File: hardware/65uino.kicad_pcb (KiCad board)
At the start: 2 copper layers, 75.4 x 53.6 mm, 50 parts, among them J1 Barrel_Jack_MountingPin, J2 USB_B_Micro, J3 OLED, SW1 RST, SW2 BTN, U1 R6507, U2 74HC04, U3 6532, U4 w27C512, U5 MIC5504-3.3YM5, U6 LM1117-5.0, X1 NC, Y1 1Mhz

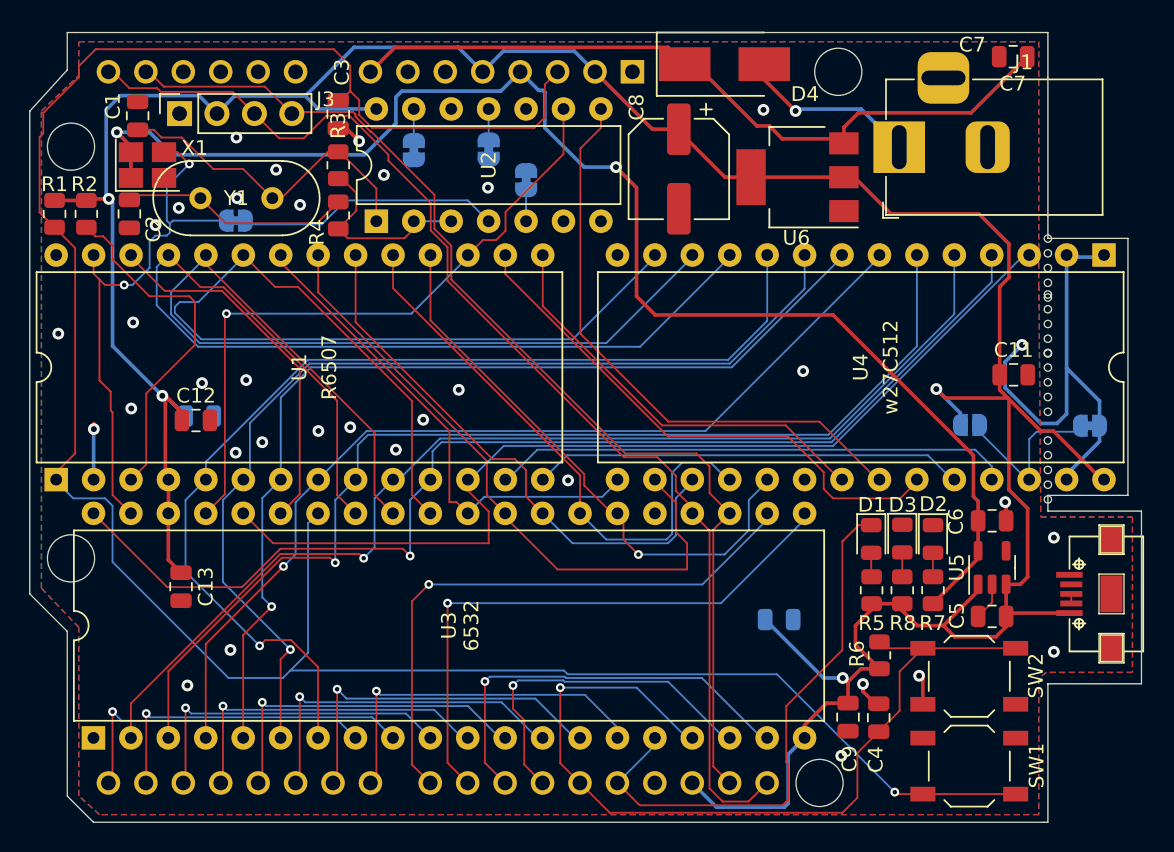
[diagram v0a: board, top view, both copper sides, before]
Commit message: SSD1306 routines + BMP180
This update adds the basic routines needed to output text to an SSD1306 OLED display, including a font.
Current state outputs a welcome text and updates the displayed raw BMP180 sensor temp data every loop tick.
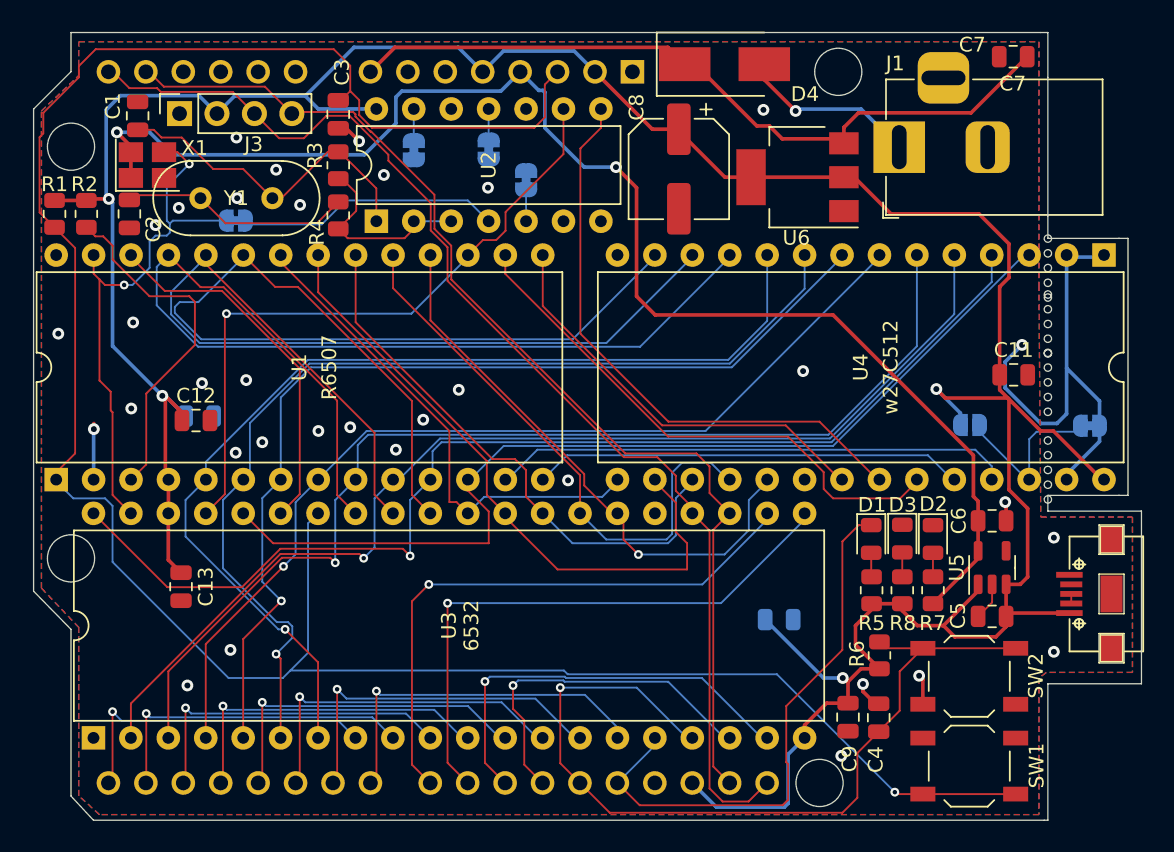
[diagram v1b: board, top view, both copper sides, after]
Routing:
- net A0: track 71.2 -> 69.7 mm
- net A1: track 67.9 -> 68.7 mm
- net A2: track 66.7 -> 67.3 mm
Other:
- board size 75.4 x 53.6 mm -> 75.2 x 53.5 mm

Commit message: Net names, silkscreen, software serial
Spoilers! :)
This has some hardware improvements but the gerber files haven't been updated this time (plot them from KiCAD).
There's also a spoiler for a future video: Software serial receives characters and outputs to screen.
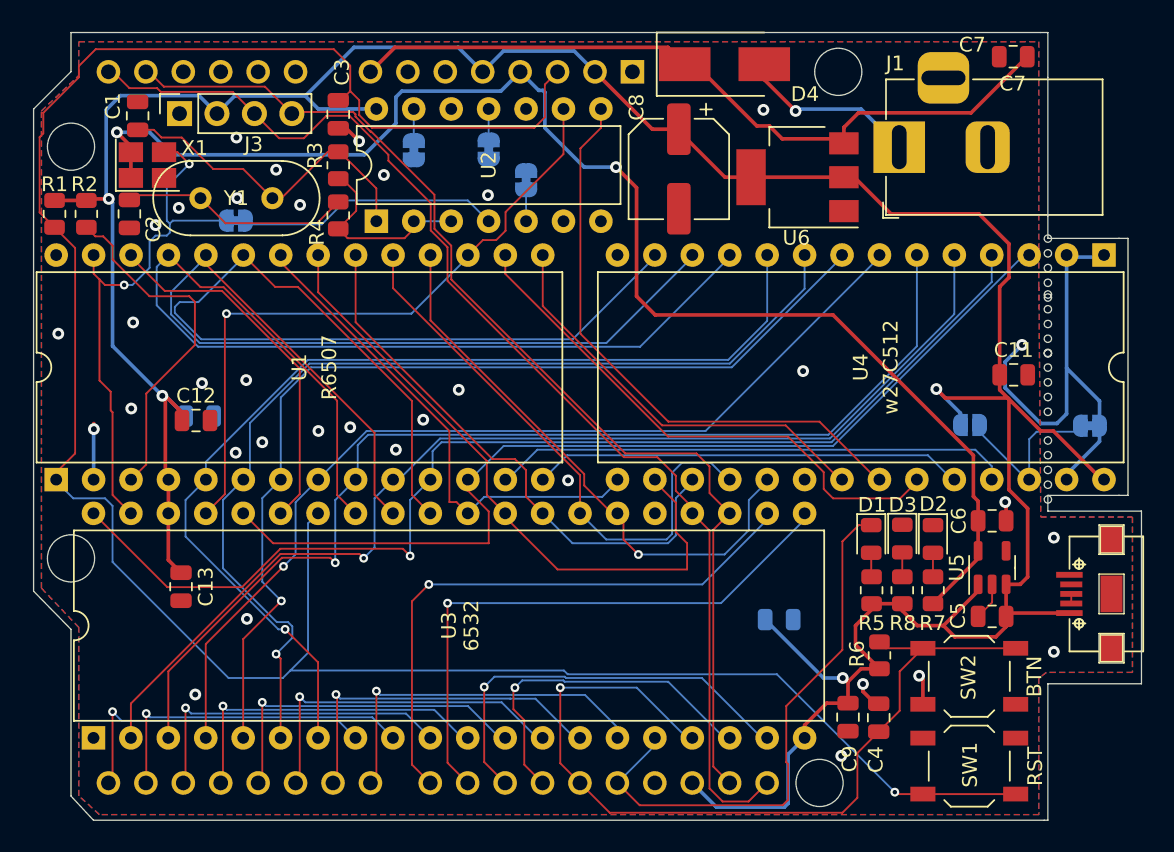
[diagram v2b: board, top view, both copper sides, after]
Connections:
- net Net-(A1-Pad15) renamed /PA0/D0/RX
- net Net-(A1-Pad16) renamed /PA1/D1/TX
- net Net-(A1-Pad17) renamed /PA2/D2
- net Net-(A1-Pad18) renamed /PA3/D3
- net Net-(A1-Pad19) renamed /PA4/D4
- net Net-(A1-Pad20) renamed /PA5/D5
- net Net-(A1-Pad21) renamed /PA6/D6
- net Net-(A1-Pad22) renamed /PA7/D7
- net Net-(A1-Pad23) renamed /PB2/D8
- net Net-(A1-Pad24) renamed /PB3/D9
- net Net-(A1-Pad25) renamed /PB4/D10
- net Net-(A1-Pad26) renamed /PB5/D11
- net Net-(A1-Pad27) renamed /PB6/D12
- net Net-(A1-Pad28) renamed /PB7/D13
- net Net-(A1-Pad3) renamed /RST
- net Net-(A1-Pad8) renamed /VIN
- net Net-(U1-Pad27) renamed /PHI0
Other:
- board text added: "3V3"
- board text added: "5V"
- board text added: "GND"
- board text added: "NC"
- board text added: "PA0 D0 RX"
- board text added: "PA1 D1 TX"
- board text added: "PA2 D2"
- board text added: "PA3 D3"
- board text added: "PA4 D4"
- board text added: "PA5 D5"
- board text added: "PA6 D6"
- board text added: "PA7 D7"
- board text added: "PB0 SCL"
- board text added: "PB1 SDA"
- board text added: "PB2 D8"
- board text added: "PB3 D9"
- board text added: "PB4 D10"
- board text added: "PB5 D11"
- board text added: "PB6 D12 BTN"
- board text added: "PB7 D13 LED"
- board text added: "PHI0"
- board text added: "RST"
- board text added: "SCL"
- board text added: "SDA"
- board text added: "VIN"

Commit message: 68.6mm
Edge cuts
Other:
- board size 75.2 x 53.5 mm -> 74.9 x 53.3 mm
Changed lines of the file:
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@@
   (gr_line (start 117.2972 95.5802) (end 118.618 94.107) (layer "B.SilkS") (width 0.1))
   (gr_line (start 175.6156 79.8068) (end 176.2252 79.8068) (layer "Edge.Cuts") (width 0.05))
-  (gr_line (start 170.7896 92.5932) (end 170.7896 101.854) (layer "Edge.Cuts") (width 0.05))
+  (gr_line (start 170.5356 92.329) (end 170.5356 101.854) (layer "Edge.Cuts") (width 0.05))
   (gr_line (start 104.4956 100.2132) (end 104.4956 88.9) (layer "Edge.Cuts") (width 0.05))
-  (gr_line (start 170.7896 60.8432) (end 170.7896 62.3672) (layer "Edge.Cuts") (width 0.05))
-  (gr_line (start 170.2816 48.3972) (end 170.7896 48.3972) (layer "Edge.Cuts") (width 0.05))
+  (gr_line (start 170.5356 60.8432) (end 170.5356 62.3672) (layer "Edge.Cuts") (width 0.05))
+  (gr_line (start 170.2816 48.514) (end 170.5356 48.514) (layer "Edge.Cuts") (width 0.05))
   (gr_line (start 101.9556 53.594) (end 104.4956 51.054) (layer "Edge.Cuts") (width 0.05))
-  (gr_line (start 177.1396 80.8736) (end 170.7896 80.8736) (layer "Edge.Cuts") (width 0.05))
+  (gr_line (start 176.8856 80.8736) (end 170.5102 80.8736) (layer "Edge.Cuts") (width 0.05))
   (gr_line (start 101.9556 86.3092) (end 101.9556 53.594) (layer "Edge.Cuts") (width 0.05))
-  (gr_line (start 104.4956 48.3972) (end 170.2816 48.3972) (layer "Edge.Cuts") (width 0.05))
-  (gr_line (start 170.7896 48.3972) (end 170.7896 51.4452) (layer "Edge.Cuts") (width 0.05))
+  (gr_line (start 104.49 48.53) (end 170.2816 48.514) (layer "Edge.Cuts") (width 0.05))
+  (gr_line (start 170.5356 48.514) (end 170.5356 51.6382) (layer "Edge.Cuts") (width 0.05))
   (gr_line (start 106.0196 101.854) (end 104.4956 100.2132) (layer "Edge.Cuts") (width 0.05))
   (gr_line (start 104.4956 88.9) (end 101.9556 86.3092) (layer "Edge.Cuts") (width 0.05))
-  (gr_line (start 175.6156 79.8068) (end 170.7896 79.8068) (layer "Edge.Cuts") (width 0.05))
-  (gr_line (start 104.4956 51.054) (end 104.4956 48.3972) (layer "Edge.Cuts") (width 0.05))
+  (gr_line (start 175.6156 79.8068) (end 170.5102 79.8068) (layer "Edge.Cuts") (width 0.05))
+  (gr_line (start 104.4956 51.054) (end 104.49 48.53) (layer "Edge.Cuts") (width 0.05))
   (gr_line (start 175.6156 62.3672) (end 176.2252 62.3672) (layer "Edge.Cuts") (width 0.05))
   (gr_line (start 170.5356 101.854) (end 106.0196 101.854) (layer "Edge.Cuts") (width 0.05))
-  (gr_line (start 177.1396 92.5932) (end 177.1396 80.8736) (layer "Edge.Cuts") (width 0.05))
-  (gr_line (start 170.7896 60.8432) (end 170.7896 51.4452) (layer "Edge.Cuts") (width 0.05))
+  (gr_line (start 176.8856 92.329) (end 176.8856 80.8736) (layer "Edge.Cuts") (width 0.05))
+  (gr_line (start 170.5356 60.8432) (end 170.5356 51.6382) (layer "Edge.Cuts") (width 0.05))
   (gr_line (start 176.2252 62.3672) (end 176.2252 79.8068) (layer "Edge.Cuts") (width 0.05))
-  (gr_line (start 170.7896 79.8068) (end 170.7896 80.8736) (layer "Edge.Cuts") (width 0.05))
-  (gr_line (start 170.7896 92.5932) (end 177.1396 92.5932) (layer "Edge.Cuts") (width 0.05))
-  (gr_line (start 170.7896 62.3672) (end 175.6156 62.3672) (layer "Edge.Cuts") (width 0.05))
-  (gr_line (start 170.5356 101.854) (end 170.7896 101.854) (layer "Edge.Cuts") (width 0.05))
+  (gr_line (start 170.5102 79.8068) (end 170.5102 80.8736) (layer "Edge.Cuts") (width 0.05))
+  (gr_line (start 170.5356 92.329) (end 176.8856 92.329) (layer "Edge.Cuts") (width 0.05))
+  (gr_line (start 170.5356 62.3672) (end 175.6156 62.3672) (layer "Edge.Cuts") (width 0.05))
+  (gr_line (start 170.5356 101.854) (end 170.5356 101.854) (layer "Edge.Cuts") (width 0.05))
   (gr_text "PA1\nD1\nTX" (at 110.8964 91.0844) (layer "B.SilkS")
     (effects (font (size 0.8 0.8) (thickness 0.13)) (justify mirror))

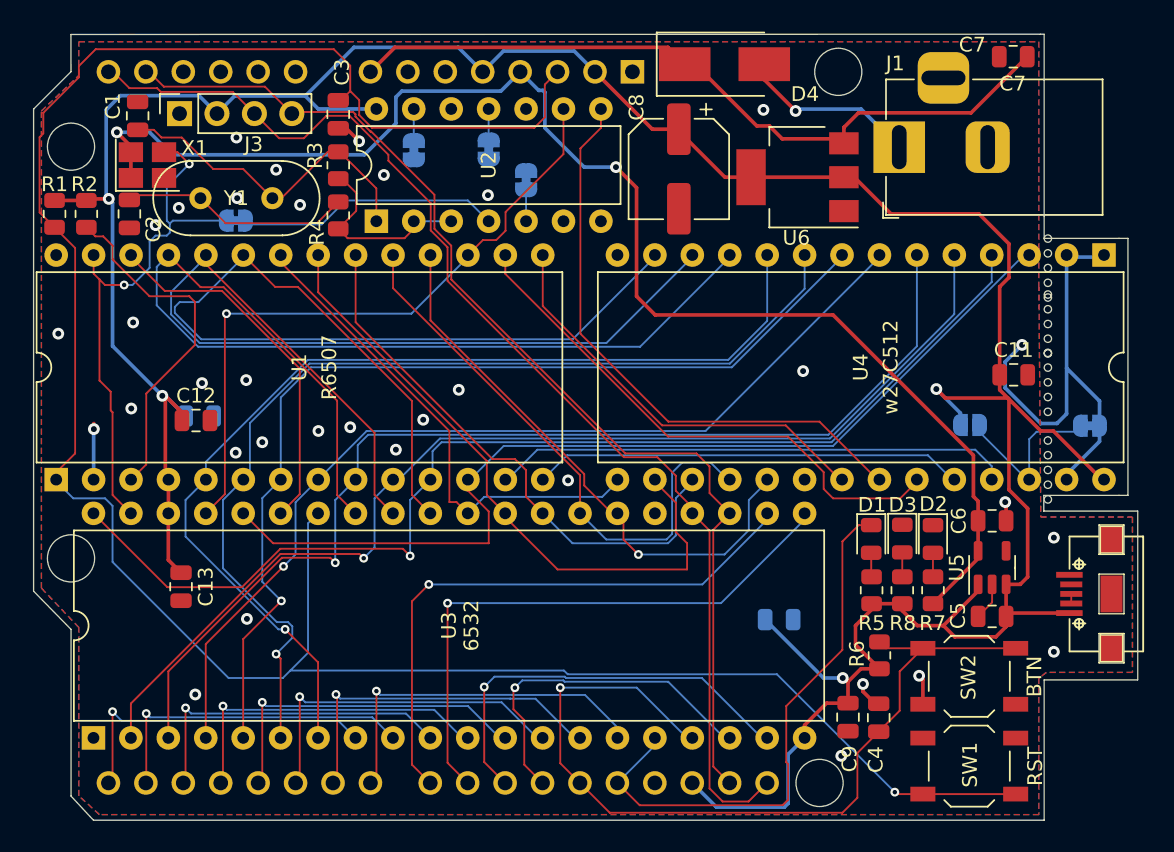
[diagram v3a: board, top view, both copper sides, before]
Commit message: Pullups on serial and i2c lines + Single gate sot23-5 inverter default
Added some "optional" pullups on the serial lines and i2c lines. Default is now to use a 1 gate sot23-5 inverter for address decoding instead of the DIP14 inverter, as well as the SMD oscillator instead of the inverter crystal oscillator circuit.
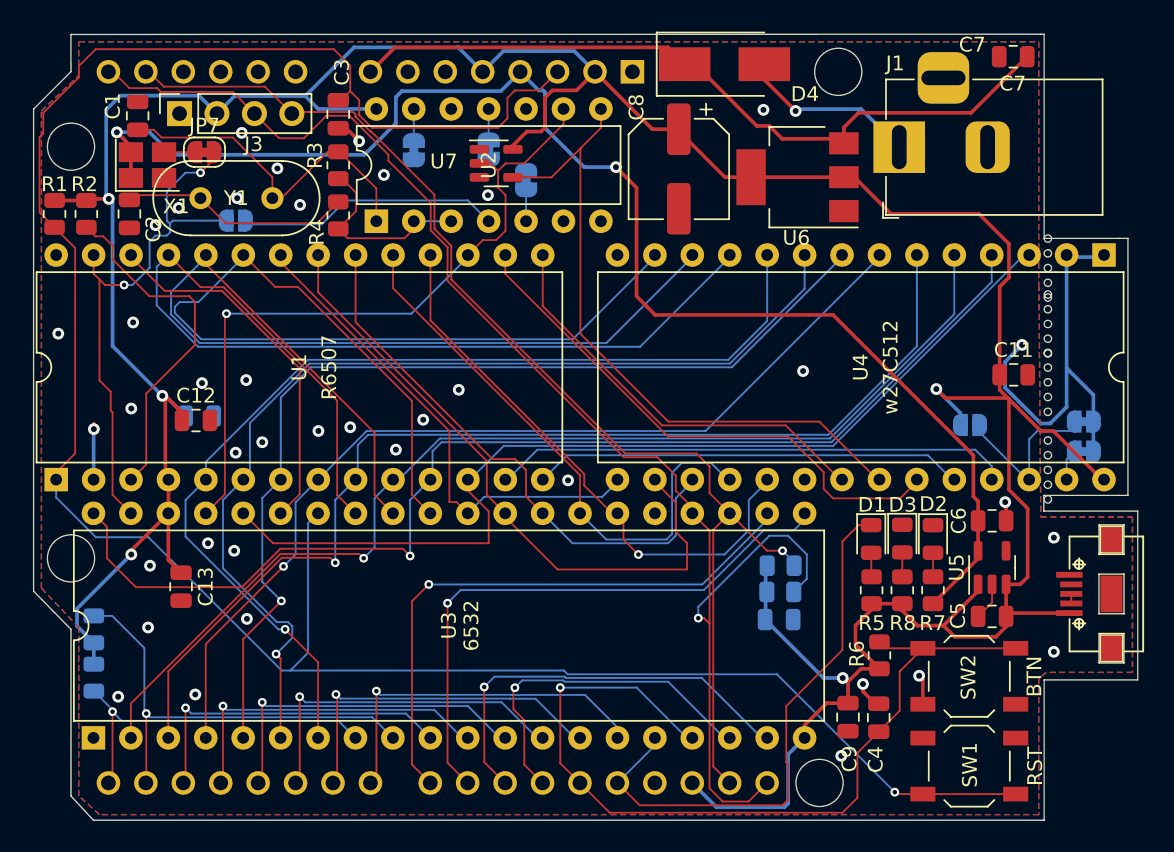
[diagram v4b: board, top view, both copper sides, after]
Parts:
- added JP7: SolderJumper_2_Bridged, Jumper:SolderJumper-2_P1.3mm_Bridged_RoundedPad1.0x1.5mm, F.Cu at (113.6, 56.5)
- added JP8: SolderJumper_2_Bridged, Jumper:SolderJumper-2_P1.3mm_Bridged_RoundedPad1.0x1.5mm, B.Cu at (173.2, 76.8)
- added R10: 22k, Resistor_SMD:R_0805_2012Metric, B.Cu at (106.0, 88.9)
- added R11: NC, Resistor_SMD:R_0805_2012Metric, B.Cu at (152.7, 84.6)
- added R12: NC, Resistor_SMD:R_0805_2012Metric, B.Cu at (152.6, 86.4)
- added R9: 22k, Resistor_SMD:R_0805_2012Metric, B.Cu at (106.0, 92.2)
- added U7: SN74LVC1G14DBVR, Package_TO_SOT_SMD:SOT-23-5, F.Cu at (133.3, 57.3)
- C1, C2: value 30pF -> NC/30pF
- JP6: footprint Jumper:SolderJumper-2_P1.3mm_Bridged_RoundedPad1.0x1.5mm -> Jumper:SolderJumper-2_P1.3mm_Open_RoundedPad1.0x1.5mm
- R3: value 1M -> NC/1M
- R4: value 470 -> NC/470
- U2: value 74HC04 -> NC/74HC04
- X1: value NC -> 1MHz
- Y1: value 1Mhz -> NC/1Mhz
- moved JP2 0.50 mm to (173.2, 74.8)
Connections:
- U4 pad 27: GND -> Net-(U4-Pad27)
- X1 pad 3: /PHI0 -> Net-(X1-Pad3)
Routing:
- net +5V: track 213.1 -> 239.2 mm, vias 4 -> 5
- net /SCL: track 80.0 -> 94.5 mm, vias 0 -> 1
- net /PA1/D1/TX: track 22.1 -> 30.9 mm
- net /SDA: track 74.8 -> 80.8 mm, vias 0 -> 1
- net Net-(U2-Pad8): track 40.3 -> 45.7 mm
- net GND: track 43.7 -> 40.8 mm, vias 34 -> 39
- net A12: track 45.2 -> 47.9 mm
- net /RST: track 158.9 -> 156.4 mm
- net Net-(U4-Pad27): track 0.00 -> 2.11 mm
- net Net-(X1-Pad3): track 0.00 -> 2.09 mm
- net /PA0/D0/RX: track 21.8 -> 23.7 mm
- net A6: track 76.9 -> 78.2 mm
- net Net-(C1-Pad1): track 21.3 -> 22.1 mm
- net Net-(JP1-Pad2): track 10.9 -> 11.4 mm

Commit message: Better SSD1306 lib, automatic bootloading and more
Better SSD1306 lib - Now does CR/NL + backspace
Automatic bootloading
Speed optimizations
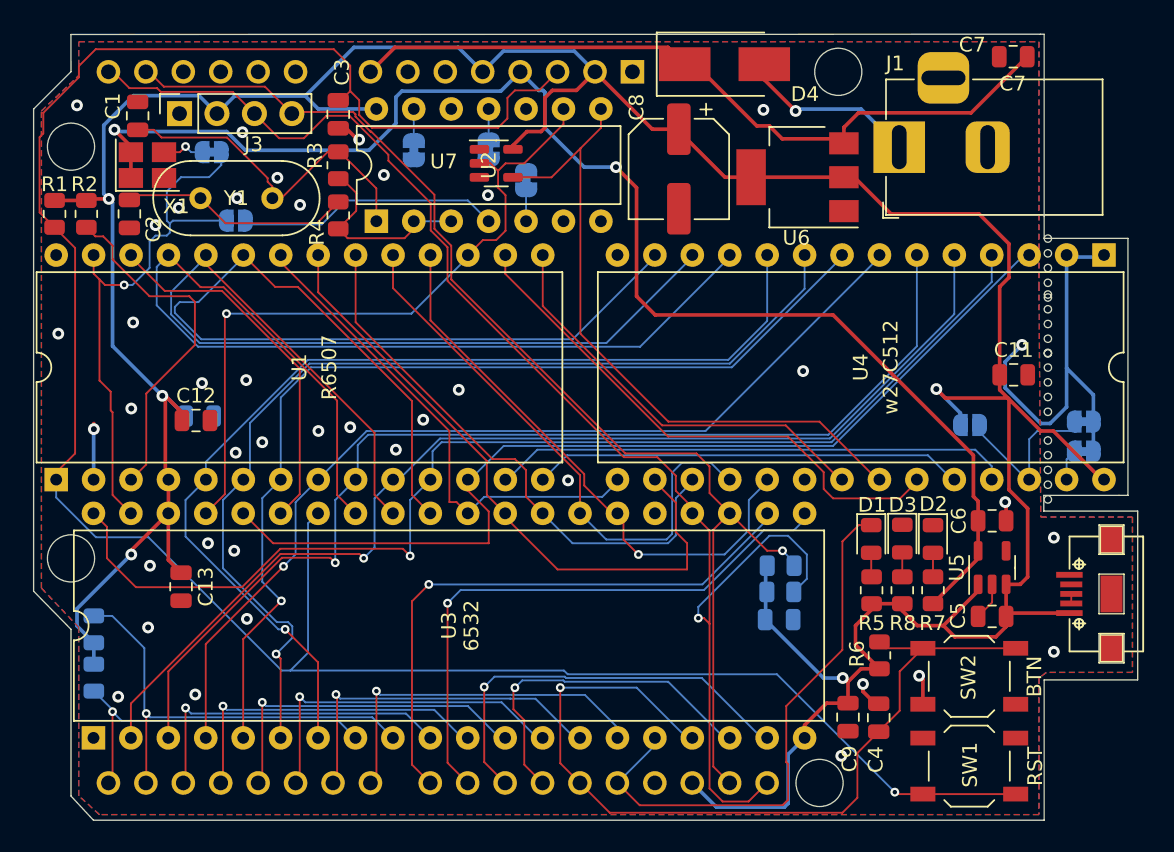
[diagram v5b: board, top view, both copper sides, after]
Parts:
- JP7: moved to B.Cu
- moved JP7 0.49 mm to (114.0, 56.5)
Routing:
- net Net-(X1-Pad3): track 2.09 -> 2.90 mm, vias 0 -> 1
- net +5V: track 239.2 -> 238.4 mm
- net /PHI0: track 37.4 -> 38.1 mm, vias 2 -> 1
- net A1: track 68.7 -> 68.0 mm
- net GND: track 40.8 -> 40.7 mm, vias 39 -> 40
